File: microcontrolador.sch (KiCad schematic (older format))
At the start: 30 parts, among them J401 Conn_01x20, J402 Conn_01x20, U401 ESP32, U402 W25Q32JVSS, Y401 26MHz, Y402 32.768kHz

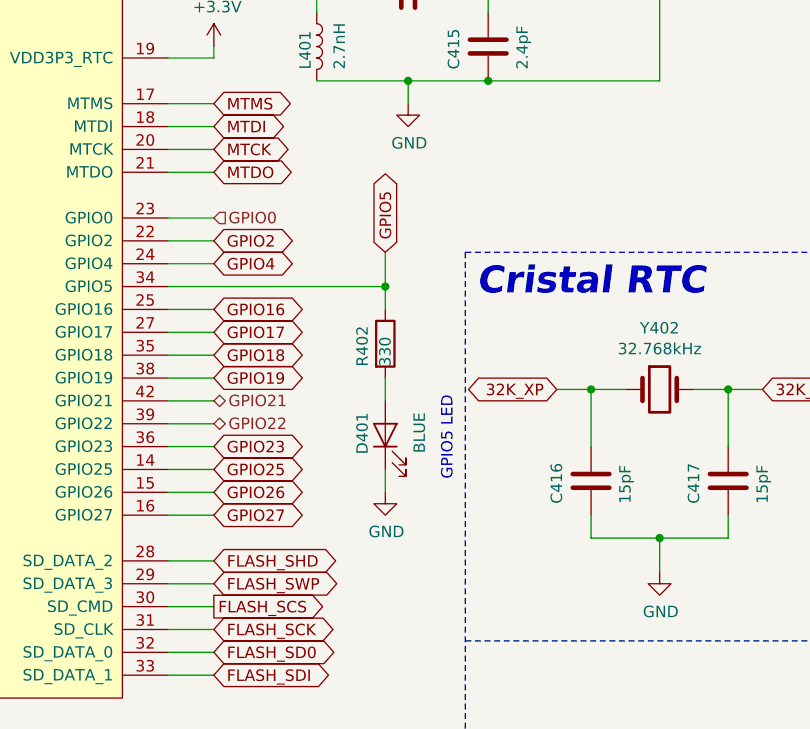
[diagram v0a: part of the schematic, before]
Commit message: PMD03 - Creacion PCB y modelo 3D
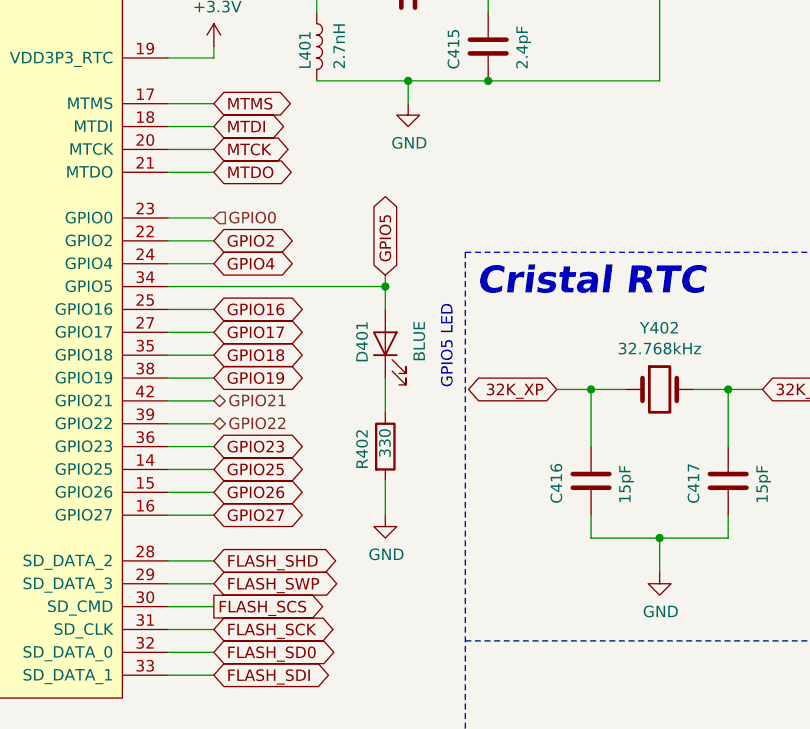
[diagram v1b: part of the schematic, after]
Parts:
- J401, J402: footprint Connector_PinHeader_1.00mm:PinHeader_1x20_P1.00mm_Vertical -> Connector_PinHeader_2.54mm:PinHeader_1x20_P2.54mm_Vertical
- U402: footprint Package_SO:SOIJ-8_5.3x5.3mm_P1.27mm -> Package_SO:SOIC-8_5.23x5.23mm_P1.27mm
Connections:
- net GND: now also R402.2; no longer D401.1 (K)
- net GPIO5: now also D401.2 (A); no longer R402.1
- new net: D401.1 (K), R402.1
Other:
- moved on the sheet: D401, R402
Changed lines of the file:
@@
 F 0 "U402" H 9500 2650 50  0000 C CNN
 F 1 "W25Q32JVSS" H 9650 1950 50  0000 C CNN
-F 2 "Package_SO:SOIJ-8_5.3x5.3mm_P1.27mm" H 9350 2300 50  0001 C CNN
+F 2 "Package_SO:SOIC-8_5.23x5.23mm_P1.27mm" H 9350 2300 50  0001 C CNN
 F 3 "http://www.winbond.com/resource-files/w25q32jv%20revg%2003272018%20plus.pdf" H 9350 2300 50  0001 C CNN
 	1    9350 2300
@@
 F 0 "J401" H 8850 3900 50  0000 L CNN
 F 1 "Conn_01x20" H 8980 4951 50  0001 L CNN
-F 2 "Connector_PinHeader_1.00mm:PinHeader_1x20_P1.00mm_Vertical" H 8900 5050 50  0001 C CNN
+F 2 "Connector_PinHeader_2.54mm:PinHeader_1x20_P2.54mm_Vertical" H 8900 5050 50  0001 C CNN
 F 3 "~" H 8900 5050 50  0001 C CNN
 	1    8900 5050
@@
 F 0 "J402" H 9550 3900 50  0000 L CNN
 F 1 "Conn_01x20" H 9680 4951 50  0001 L CNN
-F 2 "Connector_PinHeader_1.00mm:PinHeader_1x20_P1.00mm_Vertical" H 9600 5050 50  0001 C CNN
+F 2 "Connector_PinHeader_2.54mm:PinHeader_1x20_P2.54mm_Vertical" H 9600 5050 50  0001 C CNN
 F 3 "~" H 9600 5050 50  0001 C CNN
 	1    9600 5050
@@
 L Device:R R402
 U 1 1 5D6EB00B
-P 5500 3150
-F 0 "R402" V 5400 3050 50  0000 L CNN
-F 1 "330" V 5500 3050 50  0000 L CNN
-F 2 "Resistor_SMD:R_0603_1608Metric" V 5430 3150 50  0001 C CNN
-F 3 "~" H 5500 3150 50  0001 C CNN
-	1    5500 3150
-	1    0    0    -1
-$EndComp
-Text GLabel 5500 2750 1    50   BiDi ~ 0
+P 5500 3600
+F 0 "R402" V 5400 3500 50  0000 L CNN
+F 1 "330" V 5500 3550 50  0000 L CNN
+F 2 "Resistor_SMD:R_0603_1608Metric" V 5430 3600 50  0001 C CNN
+F 3 "~" H 5500 3600 50  0001 C CNN
+	1    5500 3600
+	1    0    0    -1
+$EndComp
+Text GLabel 5500 2850 1    50   BiDi ~ 0
 GPIO5
-Wire Wire Line
-	4550 2900 5500 2900
-Wire Wire Line
-	5500 2900 5500 2750
-Wire Wire Line
-	5500 3000 5500 2900
-Connection ~ 5500 2900
 $Comp
 L power:GND #PWR0402
 U 1 1 5D719F22
-P 5500 3800
-F 0 "#PWR0402" H 5500 3550 50  0001 C CNN
-F 1 "GND" H 5505 3627 50  0000 C CNN
-F 2 "" H 5500 3800 50  0001 C CNN
-F 3 "" H 5500 3800 50  0001 C CNN
-	1    5500 3800
-	1    0    0    -1
-$EndComp
-Wire Wire Line
-	5500 3400 5500 3300
-Wire Wire Line
-	5500 3800 5500 3700
+P 5500 3900
+F 0 "#PWR0402" H 5500 3650 50  0001 C CNN
+F 1 "GND" H 5505 3727 50  0000 C CNN
+F 2 "" H 5500 3900 50  0001 C CNN
+F 3 "" H 5500 3900 50  0001 C CNN
+	1    5500 3900
+	1    0    0    -1
+$EndComp
 Text GLabel 10000 4850 2    50   BiDi ~ 0
 GPIO5
-Text Notes 5800 3750 1    50   ~ 0
+Text Notes 5800 3350 1    50   ~ 0
 GPIO5 LED
 Wire Wire Line
@@
 L Device:LED D401
 U 1 1 5D6EB6DF
-P 5500 3550
-F 0 "D401" H 5600 3650 50  0000 R CNN
-F 1 "BLUE" H 5600 3400 50  0000 R CNN
-F 2 "LED_SMD:LED_0603_1608Metric" H 5500 3550 50  0001 C CNN
-F 3 "~" H 5500 3550 50  0001 C CNN
-	1    5500 3550
+P 5500 3150
+F 0 "D401" H 5600 3250 50  0000 R CNN
+F 1 "BLUE" H 5600 3000 50  0000 R CNN
+F 2 "LED_SMD:LED_0603_1608Metric" H 5500 3150 50  0001 C CNN
+F 3 "~" H 5500 3150 50  0001 C CNN
+	1    5500 3150
 	0    -1   -1   0
 $EndComp
@@
 Text Notes 6300 700  0    50   ~ 0
 Antena PCB
+Wire Wire Line
+	5500 3900 5500 3750
+Wire Wire Line
+	5500 3450 5500 3300
+Wire Wire Line
+	5500 3000 5500 2900
+Wire Wire Line
+	4550 2900 5500 2900
+Connection ~ 5500 2900
+Wire Wire Line
+	5500 2900 5500 2850
 $EndSCHEMATC

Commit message: Correcciones
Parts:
- Y401: footprint Crystal:Crystal_SMD_5032-4Pin_5.0x3.2mm -> Crystal:Crystal_SMD_5032-2Pin_5.0x3.2mm; symbol Device:Crystal_GND2_Small -> Device:Crystal
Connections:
- net GND: no longer Y401.2
- net at C406.1, U401.45 (XTAL_P): now also Y401.2; no longer Y401.3
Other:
- note added: "Accel."
- note added: "Conversion etiquetas\nglobal a local"
- note added: "Manufacturer Espressif Systems\nMfr. Part # ESP32-S0WD\nMouser Part # 356-ESP32-S0WD \nPackage # QFN-48"
- note added: "Manufacturer Windond\nMfr. Part # W25Q32JVSSIQ\nMouser Part # 454-W25Q32JVSSIQ\nPackage # SOIC-8"
- note added: "Power"

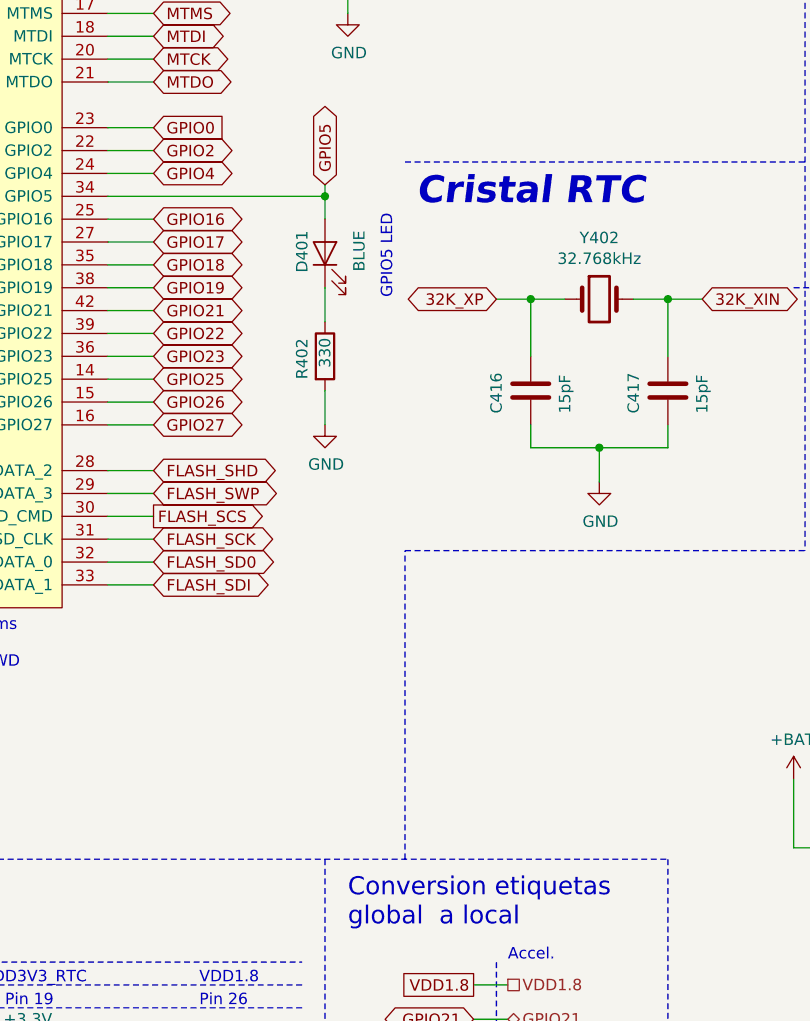
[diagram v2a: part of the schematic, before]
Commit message: Cambio en esquematico
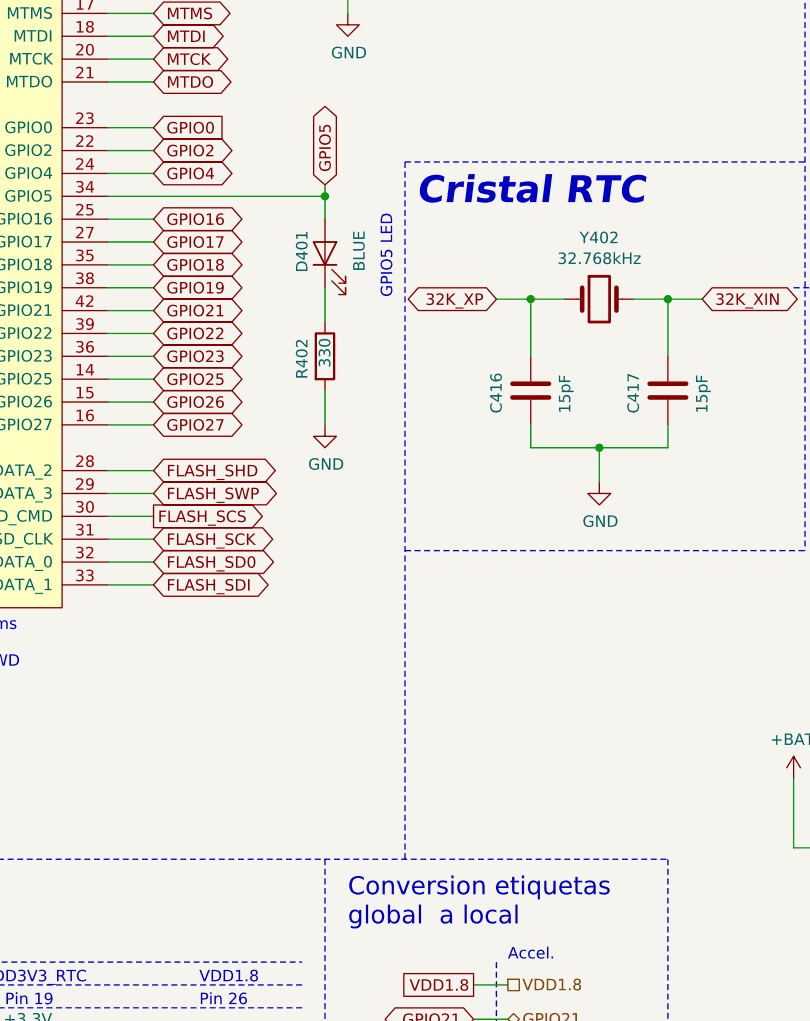
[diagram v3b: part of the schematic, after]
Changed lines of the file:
@@
 	6150 7650 6300 7650
-Wire Notes Line
-	5850 5800 5850 4450
 Wire Notes Line
 	500  5800 7000 5800
@@
 Wire Wire Line
 	1400 4000 1400 4100
+Wire Notes Line
+	5850 2750 5850 5800
 $EndSCHEMATC
